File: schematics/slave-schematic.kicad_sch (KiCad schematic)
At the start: 5 parts

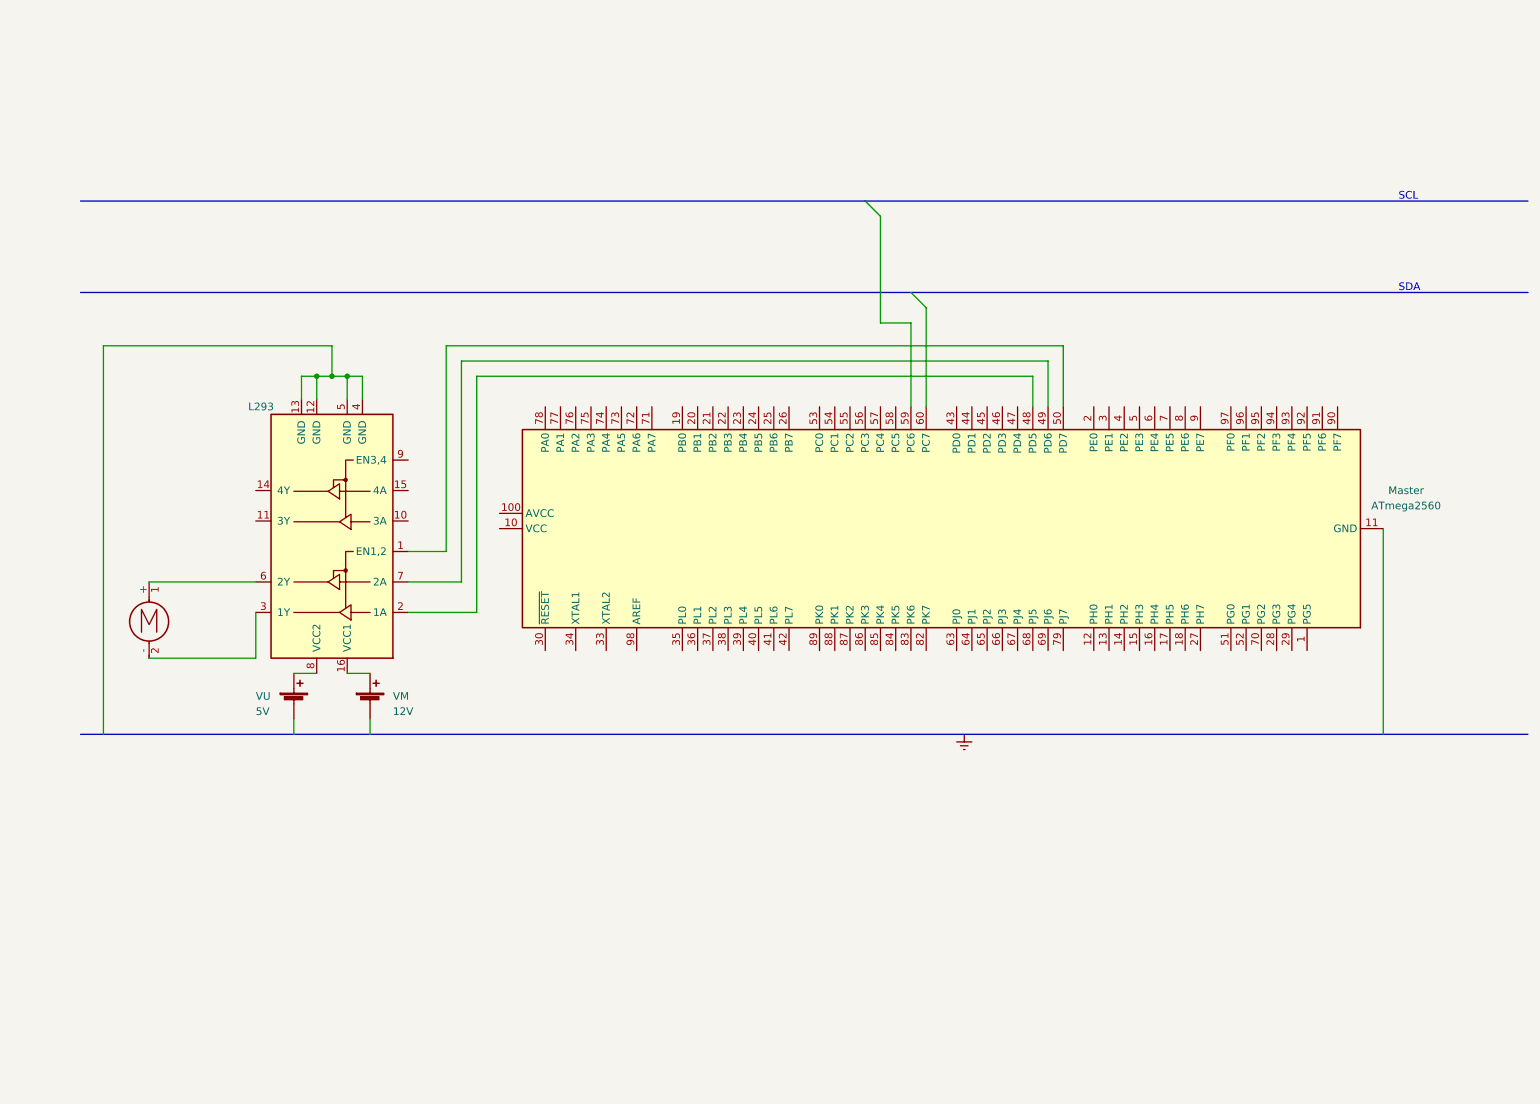
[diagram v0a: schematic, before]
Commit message: Improved schematics and added examination data
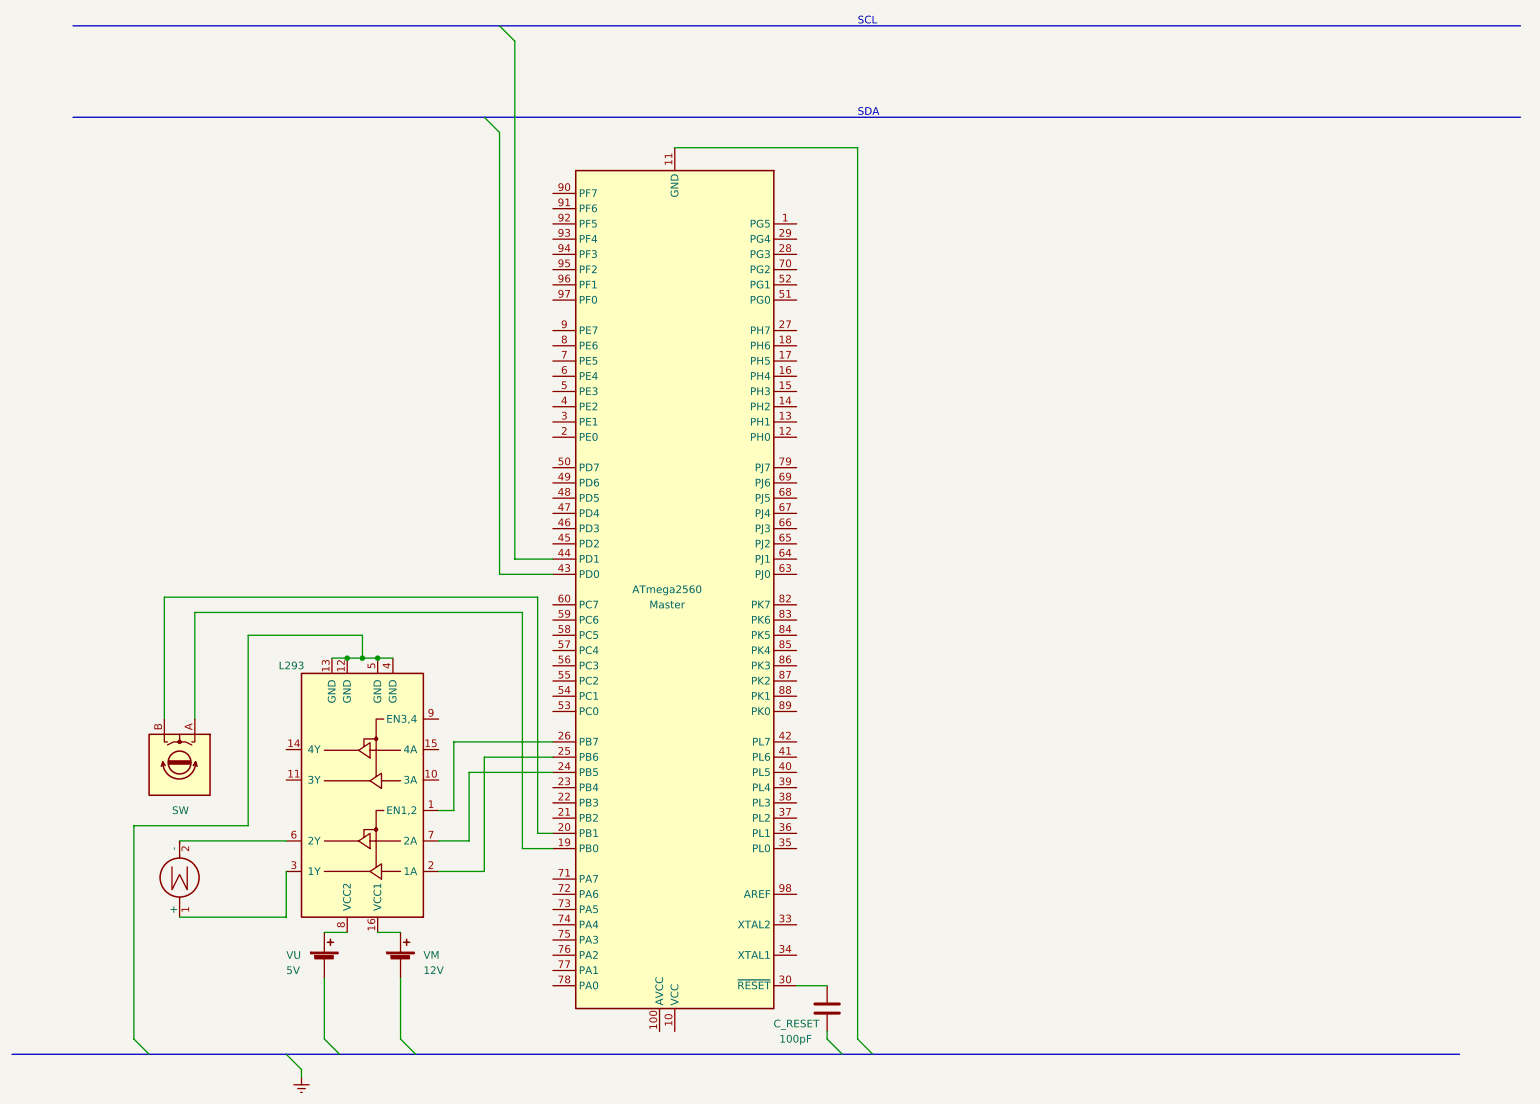
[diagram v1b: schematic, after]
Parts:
- added C_RESET: 100pF, symbol Device:C
- added SW: RotaryEncoder, symbol Device:RotaryEncoder
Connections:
- net at M.1 (+): now also U?.3 (1Y); no longer U?.6 (2Y)
- net at M.2 (-): now also U?.6 (2Y); no longer U?.3 (1Y)
- net at Master.19 (PB0): now also SW.A
- net at Master.20 (PB1): now also SW.B
- net at Master.24 (PB5): now also U?.7 (2A)
- net at Master.25 (PB6): now also U?.2 (1A)
- net at Master.26 (PB7): now also U?.1 (EN1,2)
- net at Master.30 (~{RESET}): now also C_RESET.1
- net at Master.48 (PD5): no longer U?.2 (1A)
- net at Master.49 (PD6): no longer U?.7 (2A)
- net at Master.50 (PD7): no longer U?.1 (EN1,2)
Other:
- moved on the sheet: Master, VM, VU
